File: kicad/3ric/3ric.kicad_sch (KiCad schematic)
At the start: 4 parts

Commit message: schematic updates
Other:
- note added: "3RIC 4/25/2024"
- note removed: "3RIC 2/21/2024"
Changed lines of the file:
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@@
 	(generator_version "8.0")
 	(paper "A4")
-	(text "3RIC 2/21/2024"
+	(text "3RIC 4/25/2024"
 		(exclude_from_sim no)
 		(at 189.23 177.8 0)
@@
 	)
 	(sheet
-		(at 147.32 110.49)
-		(size 30.48 15.24)
+		(at 105.41 135.89)
+		(size 33.02 15.24)
 		(fields_autoplaced yes)
 		(stroke
@@
 		)
 		(property "Sheetname" "LowRes"
-			(at 147.32 109.7784 0)
+			(at 105.41 135.1784 0)
 			(effects
 				(font
@@
 		)
 		(property "Sheetfile" "LowRes.kicad_sch"
-			(at 147.32 126.3146 0)
-			(effects
-				(font
+			(at 105.41 151.7146 0)
+			(effects
+				(font

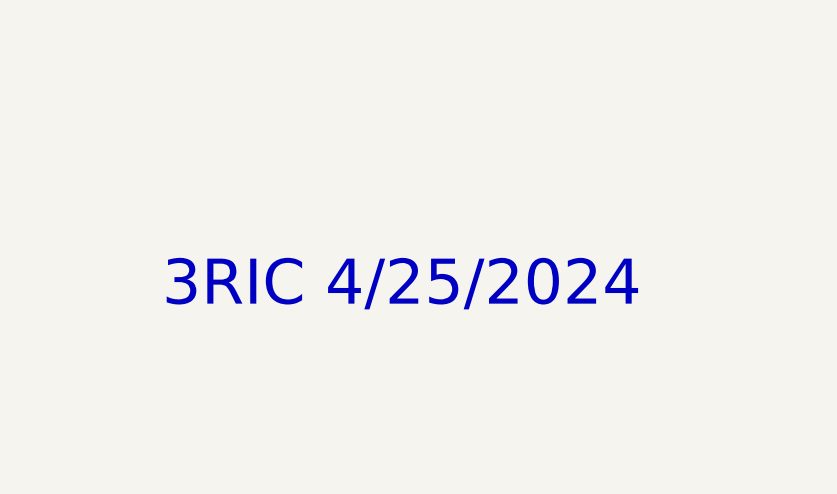
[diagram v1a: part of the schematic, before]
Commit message: update the breadboard map and the schematics
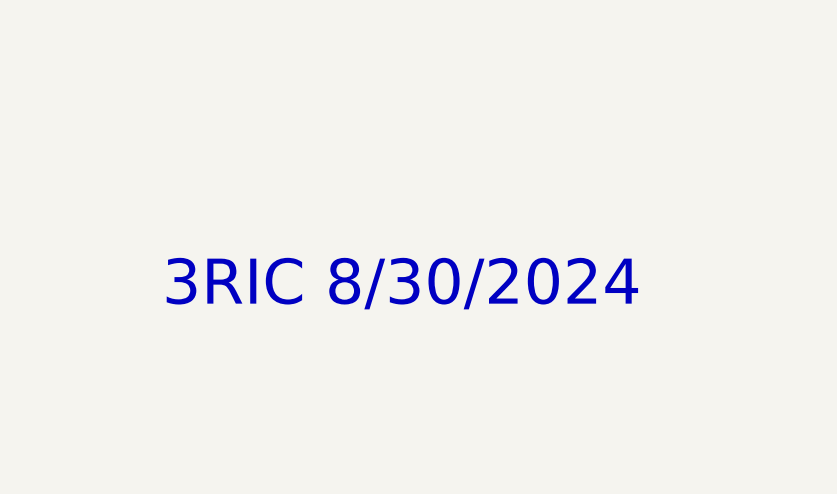
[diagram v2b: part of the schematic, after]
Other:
- note added: "3RIC 8/30/2024"
- note removed: "3RIC 4/25/2024"
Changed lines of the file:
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@@
 	(generator_version "8.0")
 	(paper "A4")
-	(text "3RIC 4/25/2024"
+	(text "3RIC 8/30/2024"
 		(exclude_from_sim no)
 		(at 189.23 177.8 0)

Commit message: update units for soft switch logic to match breadboard
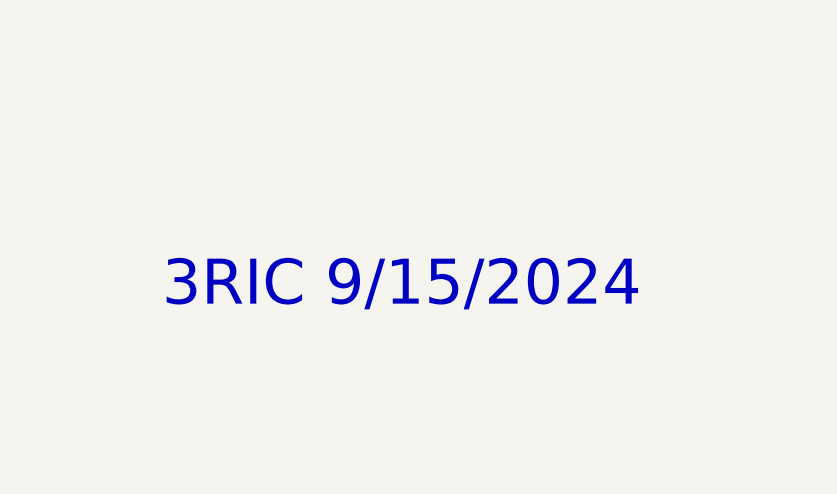
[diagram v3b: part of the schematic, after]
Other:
- note added: "3RIC 9/15/2024"
- note removed: "3RIC 8/30/2024"
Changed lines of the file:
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@@
 	(generator_version "8.0")
 	(paper "A4")
-	(text "3RIC 8/30/2024"
+	(text "3RIC 9/15/2024"
 		(exclude_from_sim no)
 		(at 189.23 177.8 0)

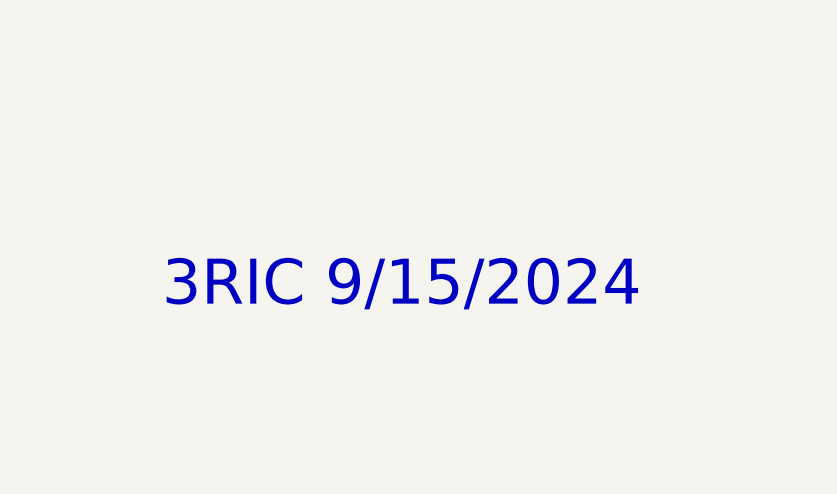
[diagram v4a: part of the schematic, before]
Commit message: update the date in the schematic and pdf
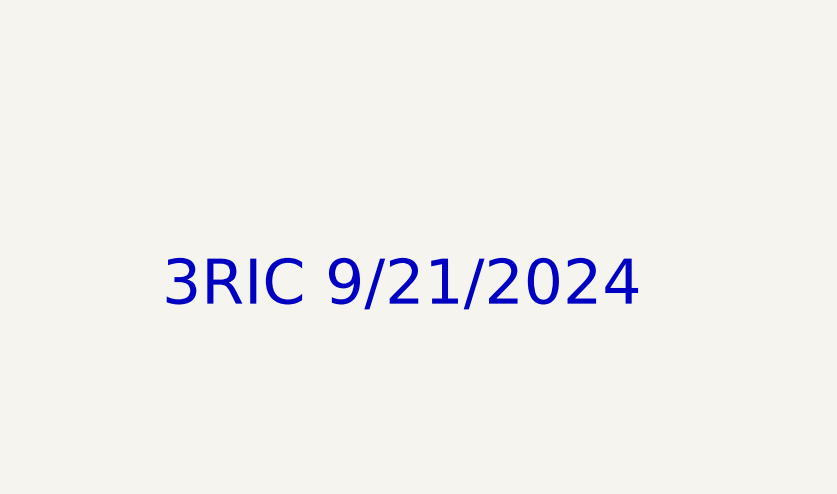
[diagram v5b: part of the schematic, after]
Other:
- note added: "3RIC 9/21/2024"
- note removed: "3RIC 9/15/2024"
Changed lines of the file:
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@@
 	(generator_version "8.0")
 	(paper "A4")
-	(text "3RIC 9/15/2024"
-		(exclude_from_sim no)
+	(text "3RIC 9/21/2024"
+		(exclude_from_sim yes)
 		(at 189.23 177.8 0)
 		(effects

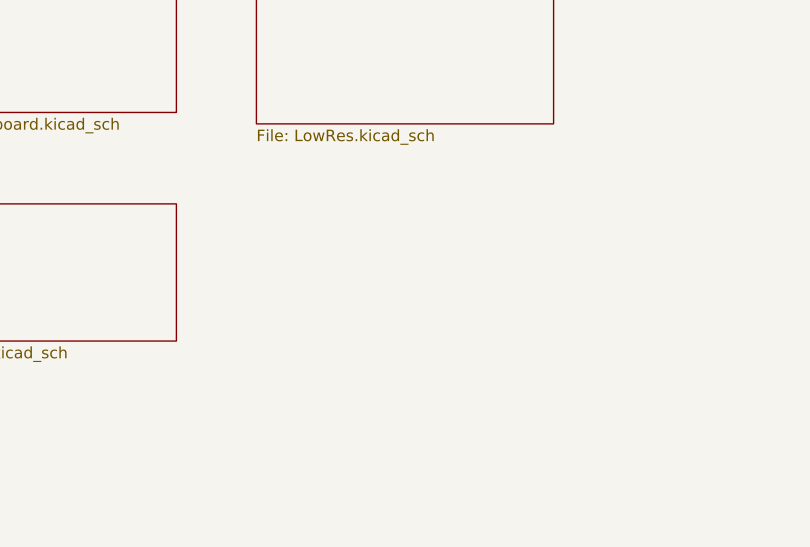
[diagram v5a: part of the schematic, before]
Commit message: completed?  Everything wired in layout creator and first draft of completed schematic
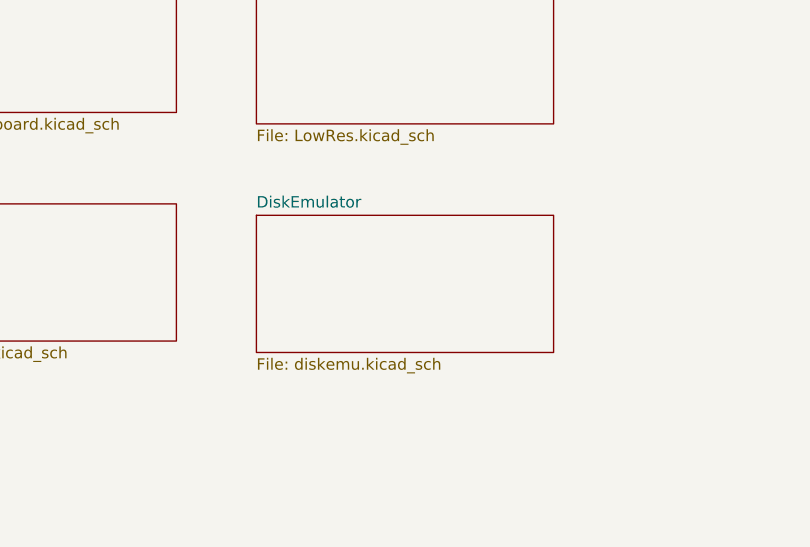
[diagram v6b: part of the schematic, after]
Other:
- added sheet DiskEmulator (diskemu.kicad_sch)
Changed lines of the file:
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@@
+	)
+	(sheet
+		(at 105.41 161.29)
+		(size 33.02 15.24)
+		(fields_autoplaced yes)
+		(stroke
+			(width 0.1524)
+			(type solid)
+		)
+		(fill
+			(color 0 0 0 0.0000)
+		)
+		(property "Sheetname" "DiskEmulator"
+			(at 105.41 160.5784 0)
+			(effects
+				(font
+					(size 1.27 1.27)
+				)
+				(justify left bottom)
+			)
+		)
+		(property "Sheetfile" "diskemu.kicad_sch"
+			(at 105.41 177.1146 0)
+			(effects
+				(font
+					(size 1.27 1.27)
+				)
+				(justify left top)
+			)
+		)
+		(instances
+			(project "3ric"
+				(path "/e63e39d7-6ac0-4ffd-8aa3-1841a4541b55"
+					(page "20")
+				)
+			)
+		)
 	)
 	(sheet

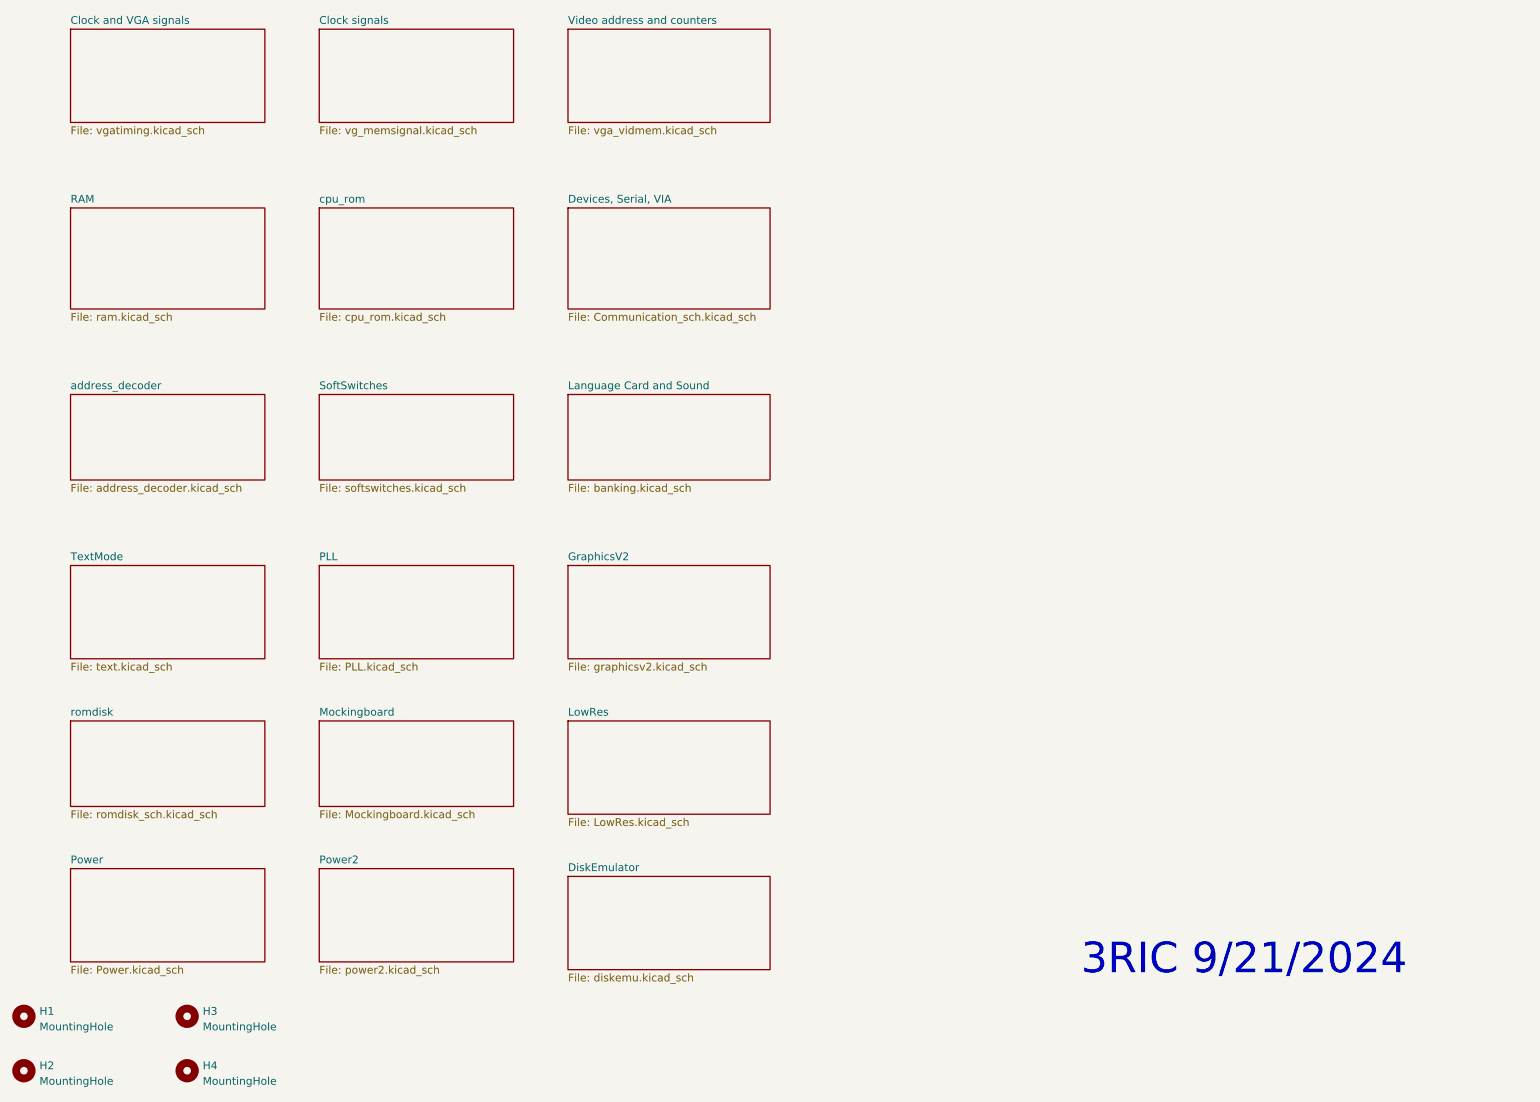
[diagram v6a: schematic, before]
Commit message: updated schematics and PCB PNG of the breadboard layout
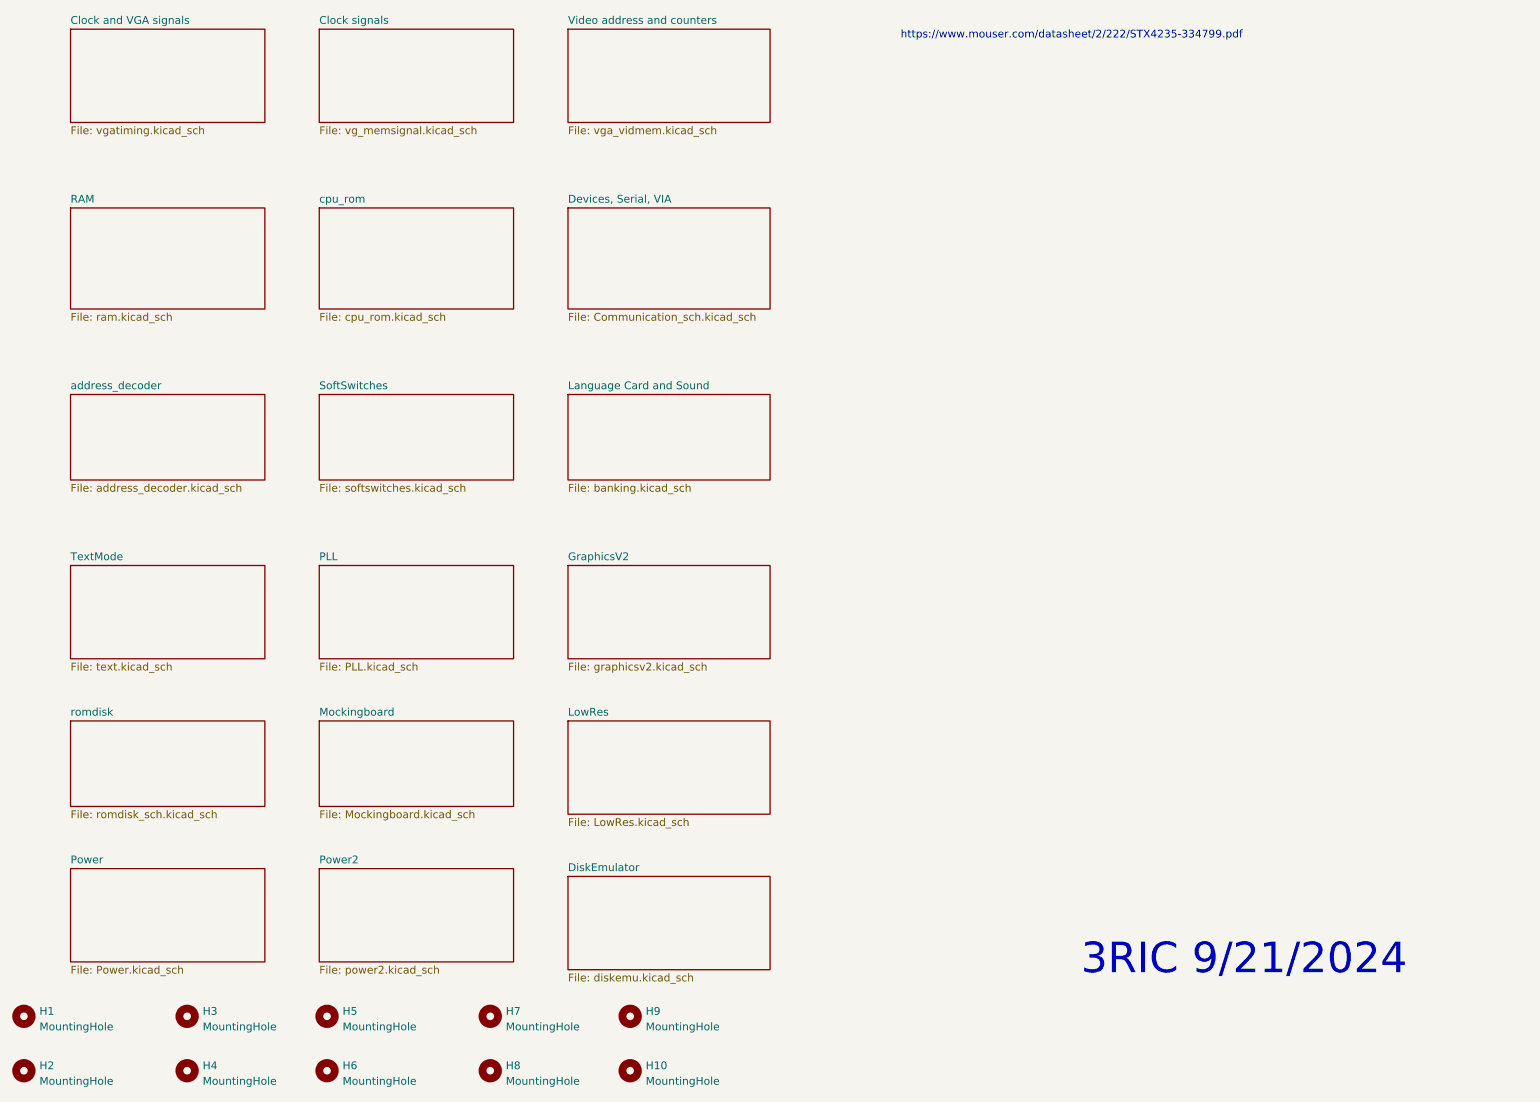
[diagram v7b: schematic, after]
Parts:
- added H10, H5, H6, H7, H8, H9: MountingHole, MountingHole:MountingHole_4.3mm_M4, symbol Mechanical:MountingHole
- H1, H2, H3, H4: footprint MountingHole:MountingHole_3.2mm_M3 -> MountingHole:MountingHole_4.3mm_M4
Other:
- note added: "https://www.mouser.com/datasheet/2/222/STX4235-334799.pdf"

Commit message: so close!  PCB ready to go?
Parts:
- H1, H10, H2, H3, H4, H5, H6, H7, H8, H9: footprint MountingHole:MountingHole_4.3mm_M4 -> MountingHole:MountingHole_3.2mm_M3_ISO14580_Pad
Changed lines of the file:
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@@
 			)
 		)
-		(property "Footprint" "MountingHole:MountingHole_4.3mm_M4"
+		(property "Footprint" "MountingHole:MountingHole_3.2mm_M3_ISO14580_Pad"
 			(at 16.51 184.15 0)
 			(effects
@@
 			)
 		)
-		(property "Footprint" "MountingHole:MountingHole_4.3mm_M4"
+		(property "Footprint" "MountingHole:MountingHole_3.2mm_M3_ISO14580_Pad"
 			(at 43.18 193.04 0)
 			(effects
@@
 			)
 		)
-		(property "Footprint" "MountingHole:MountingHole_4.3mm_M4"
+		(property "Footprint" "MountingHole:MountingHole_3.2mm_M3_ISO14580_Pad"
 			(at 92.71 193.04 0)
 			(effects
@@
 			)
 		)
-		(property "Footprint" "MountingHole:MountingHole_4.3mm_M4"
+		(property "Footprint" "MountingHole:MountingHole_3.2mm_M3_ISO14580_Pad"
 			(at 115.57 184.15 0)
 			(effects
@@
 			)
 		)
-		(property "Footprint" "MountingHole:MountingHole_4.3mm_M4"
+		(property "Footprint" "MountingHole:MountingHole_3.2mm_M3_ISO14580_Pad"
 			(at 66.04 184.15 0)
 			(effects
@@
 			)
 		)
-		(property "Footprint" "MountingHole:MountingHole_4.3mm_M4"
+		(property "Footprint" "MountingHole:MountingHole_3.2mm_M3_ISO14580_Pad"
 			(at 115.57 193.04 0)
 			(effects
@@
 			)
 		)
-		(property "Footprint" "MountingHole:MountingHole_4.3mm_M4"
+		(property "Footprint" "MountingHole:MountingHole_3.2mm_M3_ISO14580_Pad"
 			(at 43.18 184.15 0)
 			(effects
@@
 			)
 		)
-		(property "Footprint" "MountingHole:MountingHole_4.3mm_M4"
+		(property "Footprint" "MountingHole:MountingHole_3.2mm_M3_ISO14580_Pad"
 			(at 66.04 193.04 0)
 			(effects
@@
 			)
 		)
-		(property "Footprint" "MountingHole:MountingHole_4.3mm_M4"
+		(property "Footprint" "MountingHole:MountingHole_3.2mm_M3_ISO14580_Pad"
 			(at 16.51 193.04 0)
 			(effects
@@
 			)
 		)
-		(property "Footprint" "MountingHole:MountingHole_4.3mm_M4"
+		(property "Footprint" "MountingHole:MountingHole_3.2mm_M3_ISO14580_Pad"
 			(at 92.71 184.15 0)
 			(effects
